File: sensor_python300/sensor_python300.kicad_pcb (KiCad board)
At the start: 4 copper layers, 30 x 30 mm, 73 parts, among them J101 DF40HC(4.0)-60DS-0.4V(51), U101 NOIP1SN0300A-QTI, U102 TPS22918DBVR, U103 TPS22918DBVR, U104 TPS22918DBVR, U105 APX803S, X101 <DNP> DSC1103DI5-360.0000

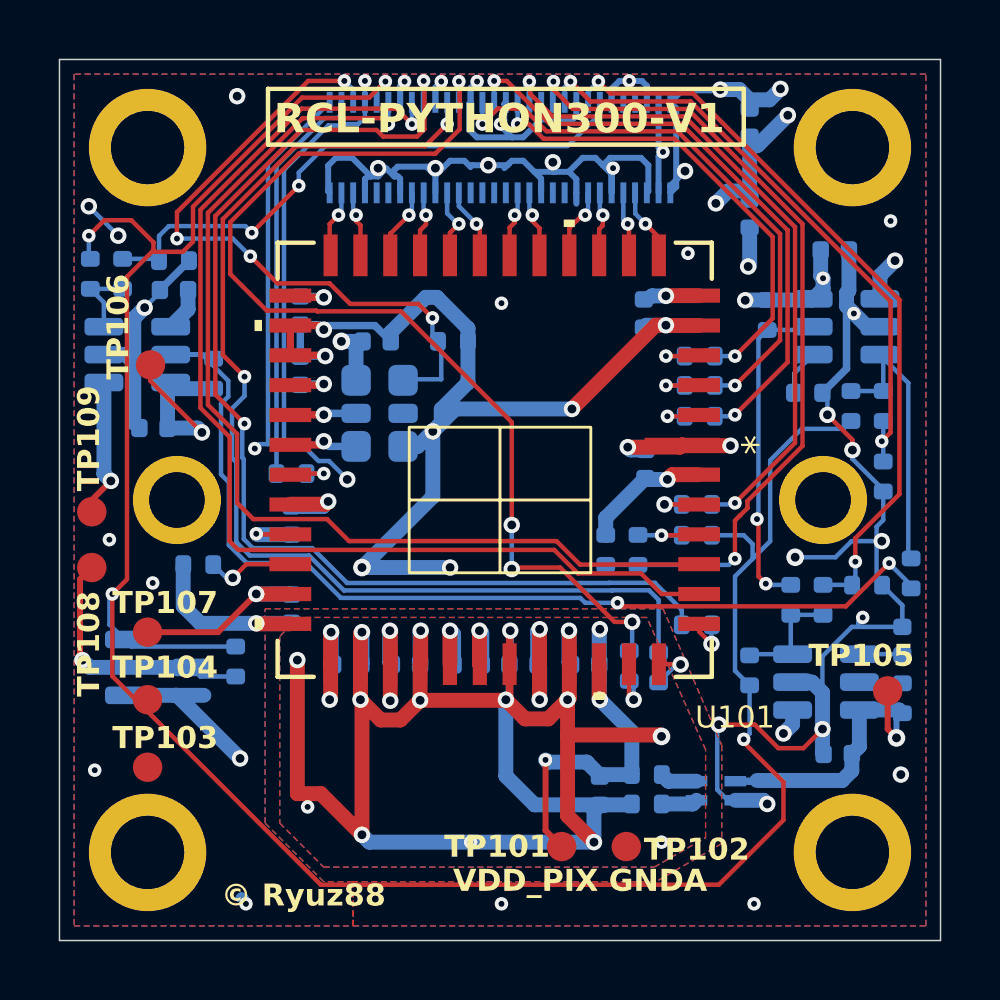
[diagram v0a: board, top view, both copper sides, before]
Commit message: 電源回路を昇圧DC-DCを使うものに変更
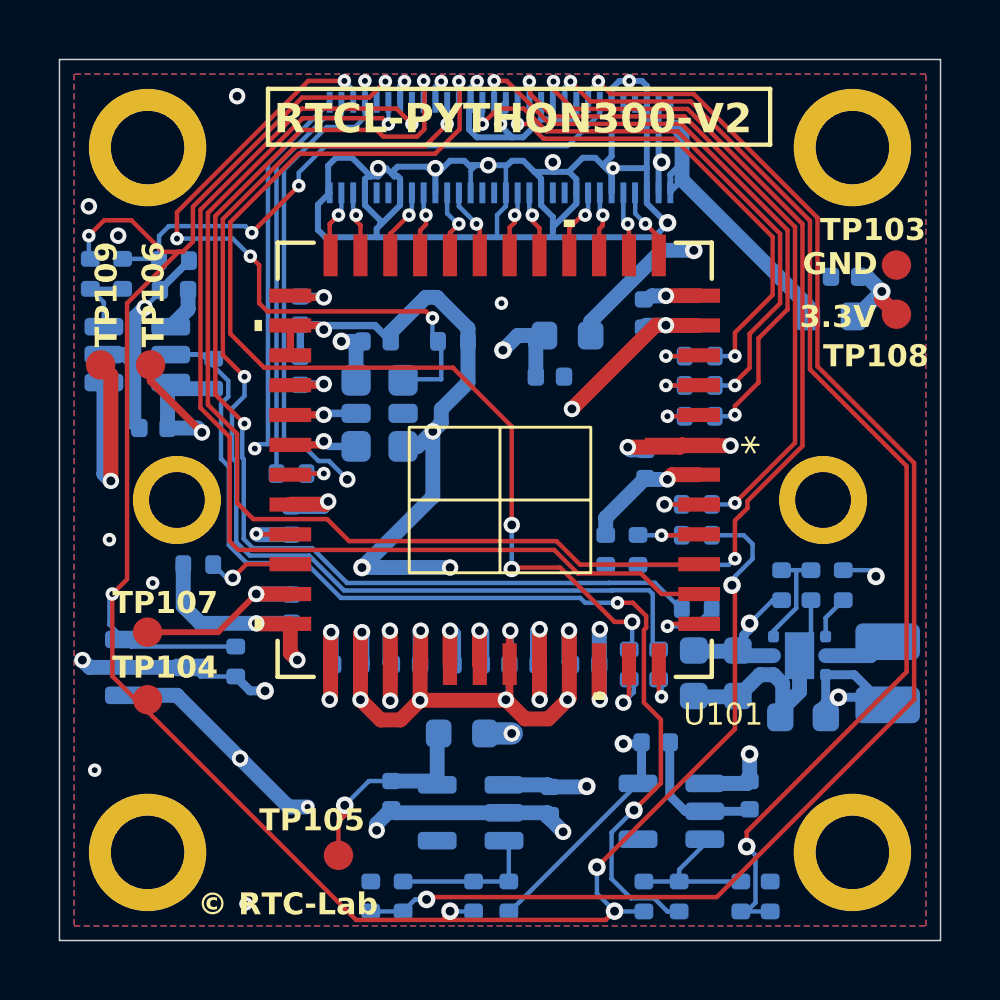
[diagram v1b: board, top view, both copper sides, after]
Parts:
- removed C115: 4.7uF, Capacitor_SMD:C_0402_1005Metric
- removed L101: EXC-24CN601X, sensor_python300:XMER_EXC-24CN601X_PAN
- removed R104: 33, Resistor_SMD:R_0402_1005Metric
- removed R105, R106: 0, Resistor_SMD:R_0402_1005Metric
- removed TP101, TP102: ~, sensor_python300:TestPin
- added C122: 10uF, Capacitor_SMD:C_0603_1608Metric, B.Cu at (160.3, 107.4)
- added C123: 10uF, Capacitor_SMD:C_0603_1608Metric, B.Cu at (156.6, 105.9)
- added C124: 10uF, Capacitor_SMD:C_0603_1608Metric, B.Cu at (158.1, 105.9)
- added FB101: BLM18AG601SN1, Inductor_SMD:L_0603_1608Metric, B.Cu at (148.7, 108.0)
- added FB102: BLM18AG601SN1, Inductor_SMD:L_0603_1608Metric, B.Cu at (161.2, 93.8)
- added FB103: BLM18AG601SN1, Inductor_SMD:L_0603_1608Metric, B.Cu at (152.3, 94.4)
- added L102: 2.2uH, Inductor_SMD:L_1008_2520Metric, B.Cu at (163.2, 105.9)
- added R131: <DNP> R, Resistor_SMD:R_0402_1005Metric, B.Cu at (159.6, 102.9)
- added R132: <DNP> R, Resistor_SMD:R_0402_1005Metric, B.Cu at (160.6, 102.9)
- added U106: TPS610995DRVR, Package_SON:WSON-6-1EP_2x2mm_P0.65mm_EP1x1.6mm, B.Cu at (160.2, 105.3)
- C101, C114: value <DNP> C -> 1uF
- C116, C117: value 4.7uF -> 1uF
- R102: value 33 -> 0
- U102, U104: value TPS22918DBVR -> TPS7A2033PDBVR; footprint Package_TO_SOT_SMD:SOT-23-6 -> Package_TO_SOT_SMD:SOT-23-5
- moved TP103 30.7 mm to (163.5, 92.0)
- moved TP108 28.7 mm to (163.5, 93.7)
- moved R111 19.9 mm to (145.6, 113.5), turned to 90 degrees
- moved TP105 19.5 mm to (144.5, 112.1)
- moved R117 18.1 mm to (154.9, 113.5)
- moved C117 17.8 mm to (155.3, 108.2)
- moved U104 17.5 mm to (155.8, 110.6)
- moved R115 17.5 mm to (146.7, 113.5), turned to 90 degrees
- moved R107 17.4 mm to (158.2, 113.5)
- moved C116 15.3 mm to (146.3, 110.0), turned to -90 degrees
- moved R120 14.8 mm to (159.2, 113.5), turned to 90 degrees
- moved R114 13.9 mm to (150.3, 113.5), turned to -90 degrees
- moved C114 13.8 mm to (158.5, 110.0), turned to -90 degrees
- moved R116 13.5 mm to (156.1, 113.5)
- moved C101 13.2 mm to (151.7, 110.2), turned to -90 degrees
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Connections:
- C101 pad 1: Net-(U102-CT) -> +3V6
- C103 pad 2: GNDA -> GND
- C104 pad 2: GNDA -> GND
- C105 pad 2: GNDA -> GND
- C106 pad 2: GNDA -> GND
- C114 pad 1: Net-(U104-CT) -> +3V6
- J101 pad 1: +3.3VP -> /CON_V33
- J101 pad 2: +1V8 -> /CON_V18
- J101 pad 31: +3.3VP -> /CON_V33
- J101 pad 32: +1V8 -> /CON_V18
- R102 pad 1: /PGOOD_PIX -> +3.3VP
- R102 pad 2: +3.3VA -> Net-(U106-EN)
- R114 pad 2: /PGOOD_VDD33 -> VDD_33
- U101 pad 32: GNDA -> GND
- U101 pad 34: GNDA -> GND
- U101 pad 37: GNDA -> GND
- U101 pad 39: GNDA -> GND
- U102 pad 1: +3.3VP -> +3V6
- U102 pad 4: Net-(U102-CT) -> unconnected-(U102-N/C-Pad4)
- U102 pad 5: /PGOOD_PIX -> +3.3VA
- U104 pad 1: +3.3VP -> +3V6
- U104 pad 4: Net-(U104-CT) -> unconnected-(U104-N/C-Pad4)
- U104 pad 5: /PGOOD_VDD33 -> VDD_33
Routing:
- net GNDA: track 99.7 -> 0.00 mm, vias 15 -> 0
- net +3.3VP: track 88.0 -> 60.8 mm, vias 6 -> 5
- net /PWR_EN_PIX: track 25.6 -> 49.5 mm
- net +3V6: track 0.00 -> 21.0 mm, vias 0 -> 3
- net /PWR_EN_VDD33: track 21.1 -> 39.3 mm
- net +1V8: track 40.6 -> 25.9 mm, vias 3 -> 2
- net VDD_33: track 69.3 -> 83.0 mm, vias 8 -> 7
- net /CON_V18: track 0.00 -> 11.5 mm, vias 0 -> 2
- net /PGOOD_VDD33: track 11.4 -> 0.00 mm, vias 2 -> 0
- net GND: track 360.1 -> 371.5 mm, vias 50 -> 46
- net /CON_V33: track 0.00 -> 11.0 mm
- net VDD_PIX: track 60.1 -> 52.7 mm
- net /PGOOD: track 82.1 -> 76.2 mm, vias 4 -> 7
- net Net-(U104-EN): track 9.77 -> 5.39 mm
- net Net-(U106-FB): track 0.00 -> 3.58 mm
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- added copper zone on In2.Cu, net +3V6
- removed copper zone on In1.Cu, net (none)
- removed copper zone on B.Cu, net GNDA
- removed copper zone on F.Cu, net GNDA
- removed copper zone on In1.Cu, net GNDA
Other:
- board text added: "3.3V"
- board text added: "GND"
- board text added: "RTCL-PYTHON300-V2"
- board text added: "© RTC-Lab"
- board text removed: "GNDA"
- board text removed: "RCL-PYTHON300-V1"
- board text removed: "VDD_PIX"
- board text removed: "© Ryuz88"
